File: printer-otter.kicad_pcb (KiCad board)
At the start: 4 copper layers, 42.4 x 16 mm, 45 parts, among them J1 12401610E4-2A, J2 5-20 V⎓, J3 Conn_01x14, P1 TC2030-CTX, Q1 MMBT3904, Q2 DMP3017SFG, SW2 Setup, U1 FUSB302BMPX, U2 STM32F072C8Ux, U3 AP2204R-3.3, U4 USBLC6-2SC6, U5 Si8540

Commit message: added connectors and board file
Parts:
- removed D3: B140-E3, Diode_SMD:D_SMA
- removed R14: 1k, Resistor_SMD:R_0402_1005Metric
- added C10: 0.1μF, Capacitor_SMD:C_0402_1005Metric, F.Cu at (167.5, 91.0)
- added C17: 0.1μF, Capacitor_SMD:C_0402_1005Metric, F.Cu at (178.7, 78.1)
- added C18: 0.1μF, Capacitor_SMD:C_0402_1005Metric, F.Cu at (175.6, 80.7)
- added C19: 1uF, Capacitor_SMD:C_0402_1005Metric, F.Cu at (161.7, 74.2)
- added C20: 0.1μF, Capacitor_SMD:C_0402_1005Metric, F.Cu at (175.6, 81.7)
- added C21: 0.1μF, Capacitor_SMD:C_0402_1005Metric, F.Cu at (180.9, 76.6)
- added C22: 0.1μF, Capacitor_SMD:C_0402_1005Metric, F.Cu at (166.5, 105.0)
- added C23: 0.1μF, Capacitor_SMD:C_0402_1005Metric, F.Cu at (175.6, 82.7)
- added C24: 0.1μF, Capacitor_SMD:C_0402_1005Metric, F.Cu at (177.5, 80.7)
- added C5: 0.1μF, Capacitor_SMD:C_0402_1005Metric, F.Cu at (159.1, 106.8)
- added C6: 0.1μF, Capacitor_SMD:C_0402_1005Metric, F.Cu at (165.0, 101.5)
- added C7: 1uF, Capacitor_SMD:C_0402_1005Metric, F.Cu at (173.7, 101.6)
- added D2: D_Schottky, Diode_SMD:D_SMB, F.Cu at (185.5, 63.5)
- added L1: 15µ, Inductor_SMD:L_Taiyo-Yuden_MD-4040, F.Cu at (151.9, 111.5)
- added Q3: Q_NMOS_GSD, Package_TO_SOT_SMD:SOT-23, F.Cu at (191.7, 111.4)
- added Q4: Q_PMOS_GSD, Package_TO_SOT_SMD:SOT-23, F.Cu at (188.2, 111.4)
- added SW1: Down, Button_Switch_SMD:SW_SPST_EVQP7C, F.Cu at (168.3, 71.2)
- added SW3: Up, Button_Switch_SMD:SW_SPST_EVQP7C, F.Cu at (167.5, 66.5)
- added U6: 4504, Package_SO:SOIC-16W_5.3x10.2mm_P1.27mm, F.Cu at (173.7, 56.1)
- added U7: 4504, Package_SO:SOIC-16W_5.3x10.2mm_P1.27mm, F.Cu at (173.7, 45.2)
- C1: value 1.0μF 25V -> 1uF; footprint Capacitor_SMD:C_0603_1608Metric -> Capacitor_SMD:C_0402_1005Metric
- C11, C9: value 1μF -> 1uF; footprint Capacitor_SMD:C_0603_1608Metric -> Capacitor_SMD:C_0402_1005Metric
- C13, C14, C15, C16, C4, R16: moved to F.Cu
- C2: value 2.2μF -> 1uF; footprint Capacitor_SMD:C_0603_1608Metric -> Capacitor_SMD:C_0402_1005Metric
- J2: value 5-20 V⎓ -> Conn_01x16; footprint otter:XT60_angle -> otter:Generic_FPC_0.5mm_15pin
- J3: value Conn_01x14 -> OLED_64x32; footprint Connector_Harwin:Harwin_M20-89014xx_1x14_P2.54mm_Horizontal -> otter:0.69OLED; moved to F.Cu
- P1: footprint Tag-Connect:TC2030-NL_SMALL -> Connector:Tag-Connect_TC2030-IDC-NL_2x03_P1.27mm_Vertical
- Q1: value MMBT3904 -> Q_NMOS_GSD
- Q2: value DMP3017SFG -> Q_PMOS_GSD; footprint Package_SON:Diodes_PowerDI3333-8 -> Package_TO_SOT_SMD:SOT-23
- R1, R3: value 2kΩ -> 5k1
- R10, R13, R5, R9: value 1k -> 2k
- R11, R6: value 15 -> 2k
- R12: value 10m -> 2k; footprint Resistor_SMD:R_1206_3216Metric -> Resistor_SMD:R_0402_1005Metric
- R15, R17, R7: value 2kΩ -> 2k
- R2: value 10kΩ -> 2k
- R4: value 2kΩ -> 51k
- R8: value 100kΩ -> 2k
- U1: value FUSB302BMPX -> MT3608; footprint Package_DFN_QFN:WQFN-14-1EP_2.5x2.5mm_P0.5mm_EP1.45x1.45mm -> Package_TO_SOT_SMD:SOT-23-6
- U4: value USBLC6-2SC6 -> USBLC6-4SC6
- U5: value Si8540 -> L78L09_SOT89; footprint Package_TO_SOT_SMD:SOT-23-5 -> Package_TO_SOT_SMD:SOT-89-3
- moved D4 97.6 mm to (181.5, 74.3)
- moved R10 92.1 mm to (185.9, 73.6), turned to 0 degrees
- moved Q1 91.2 mm to (198.6, 111.4), turned to 0 degrees
- moved C9 90.4 mm to (182.9, 75.6), turned to 0 degrees
- moved R9 89.4 mm to (184.0, 73.6), turned to 0 degrees
- moved U1 88.4 mm to (186.0, 90.5)
- moved C2 87.2 mm to (188.3, 70.5)
- moved Q2 82.9 mm to (195.1, 111.4), turned to 0 degrees
- moved R6 82.6 mm to (188.3, 69.5), turned to 0 degrees
- moved R17 82.0 mm to (182.9, 76.6), turned to 0 degrees
- moved D1 81.8 mm to (168.1, 89.7)
- moved R16 81.3 mm to (188.3, 71.5), turned to 0 degrees
- moved C3 77.4 mm to (184.0, 74.6), turned to 0 degrees
- moved C1 75.1 mm to (180.9, 77.6), turned to 0 degrees
- moved R7 73.3 mm to (177.5, 81.7)
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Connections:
- net /BOOT renamed Net-(JP1-Pad2)
- net /STATUS renamed Net-(R10-Pad1)
- net Net-(U2-Pad20) renamed INT_IN
- net Net-(U2-Pad26) renamed INPUT1
- net Net-(U2-Pad27) renamed INPUT2
- net Net-(U2-Pad28) renamed INDEX
- net Net-(U2-Pad29) renamed ENCODER_B
- net Net-(U2-Pad30) renamed ENCODER_A
- net Net-(U2-Pad40) renamed GPIO_ANALOG1
- net Net-(U2-Pad41) renamed GPIO_ANALOG2
- C11 pad 1: +3V3 -> VBUS
- C12 pad 1: U_OUT -> VBUS
- C3 pad 1: I_OUT -> +3V3
- J1 pad A5: CC1 -> Net-(J1-PadA5)
- J1 pad B5: CC2 -> Net-(J1-PadB5)
- J2 pad 1: /OUT -> GND
- J2 pad 2: GND -> F3_HV
- P1 pad 2: /SWDIO -> nRST
- P1 pad 3: /nRST -> GND
- P1 pad 4: /SWCLK -> Net-(P1-Pad4)
- P1 pad 5: GND -> SWCLK
- P1 pad 6: Net-(P1-Pad6) -> SWDIO
- Q1 pad 1: Net-(Q1-Pad1) -> F3
- Q2 pad 2: Net-(Q2-Pad1) -> 16V
- Q2 pad 3: Net-(Q2-Pad1) -> F3_HV
- R1 pad 1: SCL -> GND
- R1 pad 2: +3V3 -> Net-(J1-PadA5)
- R11 pad 1: Net-(R11-Pad1) -> F5
- R11 pad 2: Net-(Q2-Pad1) -> GND
- R12 pad 1: VBUS -> Net-(Q4-Pad1)
- R12 pad 2: Net-(Q2-Pad1) -> Net-(Q3-Pad3)
- R13 pad 1: VBUS -> 16V
- R13 pad 2: U_OUT -> Net-(Q4-Pad1)
- R15 pad 2: OLED_PULLUP -> +3V3
- R17 pad 2: OLED_PULLUP -> +3V3
- R3 pad 1: SDA -> GND
- R3 pad 2: +3V3 -> Net-(J1-PadB5)
- R4 pad 1: INT_N -> 16V
- R4 pad 2: +3V3 -> Net-(R4-Pad2)
- R5 pad 1: I_OUT -> Net-(R4-Pad2)
- R6 pad 1: Net-(R6-Pad1) -> F3
- R6 pad 2: VBUS -> GND
- R7 pad 1: OUT_CTL -> Net-(Q2-Pad1)
- R7 pad 2: Net-(Q1-Pad1) -> Net-(Q1-Pad3)
- R8 pad 1: VBUS -> 16V
- R8 pad 2: Net-(Q1-Pad3) -> Net-(Q2-Pad1)
- SW2 pad 2: /SETUP -> Net-(SW2-Pad2)
- U1 pad 1: CC2 -> Net-(D2-Pad2)
- U1 pad 2: VBUS -> GND
- U1 pad 3: +3V3 -> Net-(R4-Pad2)
- U1 pad 4: +3V3 -> VBUS
- U1 pad 5: INT_N -> VBUS
- U1 pad 6: SCL -> Net-(U1-Pad6)
- U2 pad 10: Net-(U2-Pad10) -> DCLK
- U2 pad 11: I_OUT -> S1
- U2 pad 12: U_OUT -> S2
- U2 pad 13: /SETUP -> S3
- U2 pad 14: Net-(U2-Pad14) -> Net-(SW2-Pad2)
- U2 pad 15: SCK -> Net-(SW3-Pad2)
- U2 pad 16: Net-(U2-Pad16) -> S4
- U2 pad 17: MOSI -> S5
- U2 pad 18: Net-(U2-Pad18) -> F3
- U2 pad 19: Net-(U2-Pad19) -> F5
- U2 pad 2: Net-(U2-Pad2) -> D1
- U2 pad 21: SCL -> UART_TX
- U2 pad 22: SDA -> UART_RX
- U2 pad 25: INT_N -> INPUT0
- U2 pad 3: Net-(U2-Pad3) -> D2
- U2 pad 34: /SWDIO -> SWDIO
- U2 pad 37: /SWCLK -> SWCLK
- U2 pad 39: OLED_PULLUP -> GPIO_ANALOG0
- U2 pad 4: Net-(U2-Pad4) -> D3
- U2 pad 45: OUT_CTL -> Net-(SW1-Pad2)
- U2 pad 46: Net-(U2-Pad46) -> CSYNC
- U2 pad 7: /nRST -> nRST
- U5 pad 1: Net-(R6-Pad1) -> 9V
- U5 pad 3: GND -> 16V
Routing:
- net +3V3: track 47.1 -> 0.00 mm, vias 11 -> 0
- net GND: track 42.9 -> 0.00 mm, vias 66 -> 0
- net VBUS: track 29.8 -> 0.00 mm, vias 11 -> 0
- net Net-(Q1-Pad3): track 21.0 -> 0.00 mm, vias 2 -> 0
- net /nRST: track 20.4 -> 0.00 mm, vias 2 -> 0
- net MOSI: track 18.8 -> 0.00 mm, vias 2 -> 0
- net SDA: track 18.4 -> 0.00 mm, vias 2 -> 0
- net SCL: track 17.5 -> 0.00 mm, vias 2 -> 0
- net /SWCLK: track 17.1 -> 0.00 mm, vias 2 -> 0
- net SCK: track 17.0 -> 0.00 mm, vias 2 -> 0
- net /SWDIO: track 14.6 -> 0.00 mm, vias 2 -> 0
- net Net-(Q1-Pad1): track 14.3 -> 0.00 mm, vias 2 -> 0
- net CC2: track 14.0 -> 0.00 mm, vias 1 -> 0
- net USB_DP: track 12.8 -> 0.00 mm
- net USB_DN: track 12.7 -> 0.00 mm, vias 2 -> 0
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- removed copper zone on In1.Cu, net +3V3
- removed copper zone on B.Cu, net /OUT
- removed copper zone on F.Cu, net /OUT
- removed copper zone on B.Cu, net GND
- removed copper zone on F.Cu, net GND
- removed copper zone on In2.Cu, net GND
- removed copper zone on B.Cu, net MOSI
- removed copper zone on F.Cu, net MOSI
- removed copper zone on F.Cu, net Net-(Q2-Pad1)
- removed copper zone on B.Cu, net SCK
- removed copper zone on In1.Cu, net VBUS
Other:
- board outline removed
- copper layers 4 -> 2
- net class Default: clearance 0.127 -> 0.2; trace_width 0.15 -> 0.25; via_dia 0.625 -> 0.8; via_drill 0.305 -> 0.4
- net class Power removed
- net class Power_Small removed
- rule pad_to_mask_clearance: 0.0635 -> 0
- rule trace_clearance: 0.127 -> 0.2
- rule trace_min: 0.15 -> 0.2
- rule via_min_drill: 0.254 -> 0.3
- rule via_min_size: 0.3 -> 0.4
- board text removed: "(roughly based on the work of Clayton G. Hobbs)"
- board text removed: "APA102"
- board text removed: "CLK"
- board text removed: "DATA"
- board text removed: "GND"
- board text removed: "POWER"
- board text removed: "STATUS"
- board text removed: "USB type C Otter Niklas Fauth 2018"
- board text removed: "VOUT"

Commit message: updated schematic, removed display and tag connect, routed board (80%)
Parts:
- removed C10, C12, C17, C3, C8: 0.1μF, Capacitor_SMD:C_0402_1005Metric
- removed C13, C14, C15, C16, C9: 1uF, Capacitor_SMD:C_0402_1005Metric
- removed J3: OLED_64x32, otter:0.69OLED
- removed P1: TC2030-CTX, Connector:Tag-Connect_TC2030-IDC-NL_2x03_P1.27mm_Vertical
- removed R15, R17: 2k, Resistor_SMD:R_0402_1005Metric
- removed R16: 560k, Resistor_SMD:R_0402_1005Metric
- removed SW2: Setup, Button_Switch_SMD:SW_SPST_EVQP7C
- removed SW3: Up, Button_Switch_SMD:SW_SPST_EVQP7C
- added J4: Encoder, Connector_PinHeader_2.54mm:PinHeader_1x05_P2.54mm_Vertical, F.Cu at (131.2, 130.0)
- added J5: UART, Connector_PinHeader_2.54mm:PinHeader_1x05_P2.54mm_Vertical, F.Cu at (105.8, 129.9)
- added J6: Analog, Connector_PinHeader_2.54mm:PinHeader_1x05_P2.54mm_Vertical, F.Cu at (134.0, 102.1)
- D2: footprint Diode_SMD:D_SMB -> Diode_SMD:D_SOD-123
- J1: value 12401610E4-2A -> USB; footprint Connector_USB:USB_C_Receptacle_Amphenol_12401548E4-2A -> badgelib:USB-C 16Pin
- J2: value Conn_01x16 -> Printer
- moved Q1 94.7 mm to (104.1, 104.8), turned to 270 degrees
- moved Q2 93.2 mm to (102.0, 107.8), turned to 90 degrees
- moved R6 91.6 mm to (105.4, 108.4), turned to 270 degrees
- moved Q3 91.0 mm to (102.1, 127.6), turned to 90 degrees
- moved U6 90.6 mm to (111.5, 122.0), turned to 90 degrees
- moved U7 89.5 mm to (111.5, 109.5), turned to 270 degrees
- moved C21 89.2 mm to (107.5, 127.2)
- moved R12 89.1 mm to (104.5, 124.9), turned to 270 degrees
- moved Q4 87.1 mm to (102.1, 124.1), turned to 270 degrees
- moved R10 82.9 mm to (121.1, 125.3), turned to 270 degrees
- moved R9 80.9 mm to (122.2, 125.8), turned to 270 degrees
- moved D4 80.9 mm to (119.7, 126.4), turned to 90 degrees
- moved R7 79.8 mm to (101.3, 105.5)
- moved R11 78.8 mm to (102.1, 129.9)
- moved D2 73.7 mm to (125.8, 106.7), turned to 90 degrees
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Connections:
- net CC1 renamed Net-(U4-Pad4)
- net CC2 renamed Net-(U4-Pad3)
- net INPUT2 renamed Net-(U2-Pad27)
- U2 pad 11: S1 -> S5
- U2 pad 17: S5 -> S1
- U2 pad 25: INPUT0 -> Net-(R10-Pad1)
- U2 pad 26: INPUT1 -> Net-(R9-Pad1)
- U2 pad 31: Net-(R9-Pad1) -> Net-(U2-Pad31)
- U2 pad 38: Net-(R10-Pad1) -> Net-(U2-Pad38)
- U6 pad 10: S4_HV -> S3_HV
- U6 pad 2: S1_HV -> S2_HV
- U6 pad 3: S1 -> S2
- U6 pad 4: S2_HV -> S4_HV
- U6 pad 5: S2 -> S4
- U6 pad 6: S3_HV -> S1_HV
- U6 pad 7: S3 -> S1
- U6 pad 9: S4 -> S3
- U7 pad 11: Net-(U7-Pad11) -> D3
- U7 pad 12: Net-(U7-Pad12) -> D3_HV
- U7 pad 2: D1_HV -> Net-(U7-Pad2)
- U7 pad 3: D1 -> Net-(U7-Pad3)
- U7 pad 4: D2_HV -> D1_HV
- U7 pad 5: D2 -> D1
- U7 pad 6: D3_HV -> D2_HV
- U7 pad 7: D3 -> D2
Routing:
- net +3V3: track 0.00 -> 85.9 mm, vias 0 -> 4
- net 16V: track 0.00 -> 46.5 mm, vias 0 -> 4
- net F3: track 0.00 -> 24.1 mm, vias 0 -> 2
- net F5: track 0.00 -> 23.7 mm, vias 0 -> 2
- net CSYNC: track 0.00 -> 18.1 mm, vias 0 -> 2
- net UART_TX: track 0.00 -> 16.3 mm, vias 0 -> 1
- net D2: track 0.00 -> 14.9 mm, vias 0 -> 2
- net UART_RX: track 0.00 -> 14.6 mm, vias 0 -> 1
- net USB_DN: track 0.00 -> 14.3 mm, vias 0 -> 2
- net ENCODER_A: track 0.00 -> 13.9 mm, vias 0 -> 1
- net D1: track 0.00 -> 13.9 mm
- net INT_IN: track 0.00 -> 13.6 mm
- net S4: track 0.00 -> 13.4 mm
- net S2: track 0.00 -> 13.3 mm, vias 0 -> 2
- net S1_HV: track 0.00 -> 13.0 mm
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- added copper zone on F.Cu, net +3V3
- added copper zone on F.Cu, net 16V
- added copper zone on F.Cu, net Net-(D2-Pad2)
- added copper zone on F.Cu, net VBUS
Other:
- board outline added: 36 x 32 mm
- board text added: "Otter"
- board text added: "Power"
- board text added: "Status"

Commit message: finalized layout
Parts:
- moved R6 4.33 mm to (104.4, 104.2)
- moved R7 3.28 mm to (104.4, 106.5), turned to 90 degrees
- moved Q1 2.06 mm to (102.1, 104.3)
- moved C22 0.93 mm to (107.5, 116.4), turned to 90 degrees
- moved R8 0.24 mm to (104.4, 108.5)
- moved C4 0.10 mm to (117.3, 112.7)
- moved Q2 0.10 mm to (102.1, 107.8)
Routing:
- net VBUS: track 13.0 -> 58.8 mm
- net +3V3: track 85.9 -> 121.1 mm, vias 4 -> 6
- net GND: track 0.00 -> 20.0 mm, vias 0 -> 56
- net Net-(SW1-Pad2): track 0.00 -> 19.6 mm, vias 0 -> 2
- net GPIO_ANALOG0: track 0.00 -> 15.5 mm, vias 0 -> 1
- net GPIO_ANALOG1: track 0.00 -> 14.1 mm, vias 0 -> 1
- net GPIO_ANALOG2: track 0.00 -> 12.8 mm, vias 0 -> 1
- net 9V: track 11.4 -> 15.3 mm
- net Net-(Q2-Pad1): track 7.22 -> 4.58 mm
- net 16V: track 46.5 -> 48.6 mm
- net F3: track 24.1 -> 26.0 mm
- net DCLK_HV: track 6.67 -> 7.92 mm
- added copper zone on B.Cu, net GND
- added copper zone on F.Cu, net GND
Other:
- net class Default: clearance 0.2 -> 0.154
- rule trace_clearance: 0.2 -> 0.154

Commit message: finalized board
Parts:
- U6, U7: footprint Package_SO:SOIC-16W_5.3x10.2mm_P1.27mm -> Package_SO:SOIC-16_3.9x9.9mm_P1.27mm
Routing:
- net +3V3: track 121.1 -> 124.5 mm
- net 9V: track 15.3 -> 16.9 mm
- net S5: track 9.49 -> 10.8 mm
- net 16V: track 48.6 -> 49.7 mm
- net S3_HV: track 12.1 -> 13.1 mm
- net S3: track 2.50 -> 3.50 mm
- net D3_HV: track 9.04 -> 9.99 mm
- net GND: track 20.0 -> 21.0 mm, vias 56 -> 58
- net S2: track 13.3 -> 12.5 mm
- net S1: track 9.29 -> 8.44 mm
- net DCLK_HV: track 7.92 -> 8.77 mm
- net DCLK: track 9.93 -> 10.8 mm
- net CSYNC_HV: track 6.23 -> 7.08 mm
- net S2_HV: track 8.69 -> 7.84 mm
- net D2_HV: track 10.3 -> 9.44 mm
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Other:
- board text added: "3V3"
- board text added: "5V"
- board text added: "@JanHenrikH"
- board text added: "A"
- board text added: "B"
- board text added: "DFU"
- board text added: "GND"
- board text added: "I"
- board text added: "INT"
- board text added: "It prints Otter!"
- board text added: "Otter-Printer"
- board text added: "PB3"
- board text added: "PB4"
- board text added: "PB5"
- board text added: "RX"
- board text added: "TX"
- board text removed: "Otter"

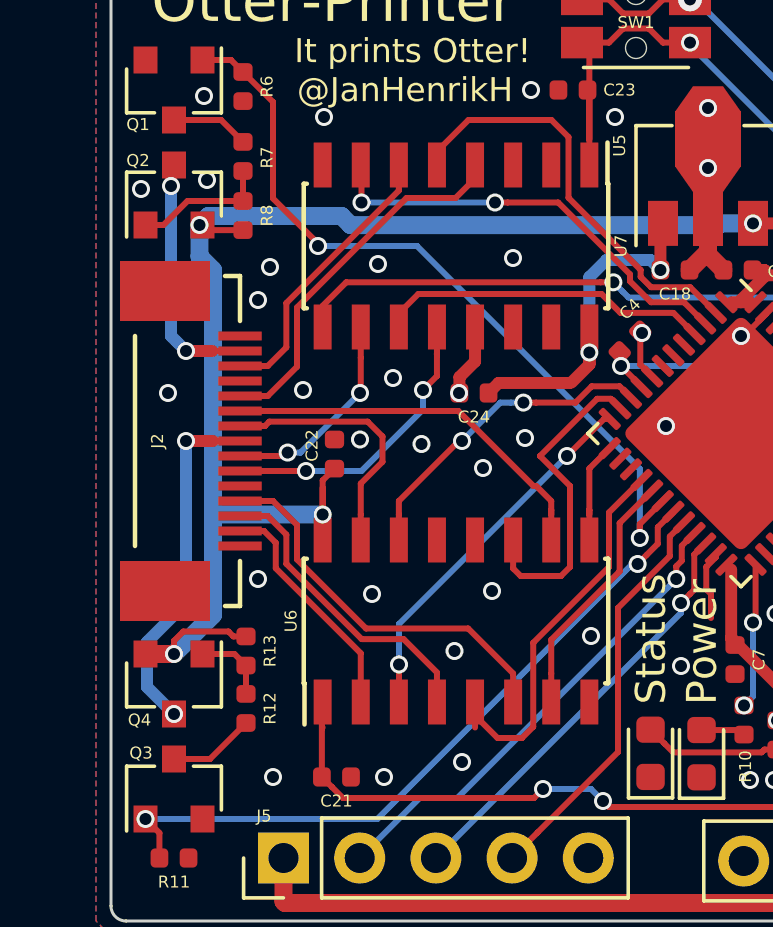
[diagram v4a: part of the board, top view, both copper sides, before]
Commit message: fixed FPC pinout
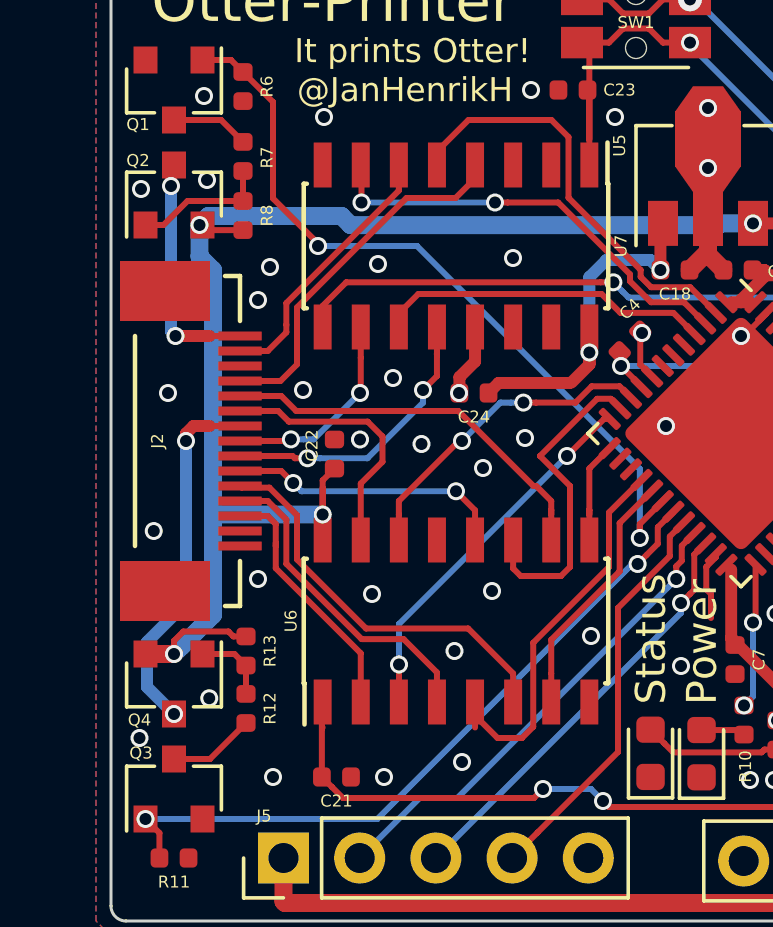
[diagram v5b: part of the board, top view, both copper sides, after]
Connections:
- J2 pad 1: GND -> F3_HV
- J2 pad 10: D3_HV -> S5_HV
- J2 pad 11: Net-(J2-Pad11) -> S1_HV
- J2 pad 12: S1_HV -> S4_HV
- J2 pad 13: S4_HV -> S2_HV
- J2 pad 14: S2_HV -> Net-(J2-Pad14)
- J2 pad 15: Net-(J2-Pad15) -> GND
- J2 pad 2: F3_HV -> D2_HV
- J2 pad 3: D2_HV -> Net-(J2-Pad3)
- J2 pad 4: Net-(J2-Pad4) -> D1_HV
- J2 pad 5: D1_HV -> S3_HV
- J2 pad 6: S3_HV -> DCLK_HV
- J2 pad 7: DCLK_HV -> F5_HV
- J2 pad 8: F5_HV -> CSYNC_HV
- J2 pad 9: CSYNC_HV -> D3_HV
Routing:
- net S5_HV: track 0.00 -> 9.37 mm, vias 0 -> 2
- net S2_HV: track 7.84 -> 8.52 mm
- net S4_HV: track 10.3 -> 10.8 mm
- net D2_HV: track 9.44 -> 8.94 mm
- net GND: vias 58 -> 61
